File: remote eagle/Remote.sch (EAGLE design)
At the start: 13 parts, among them Y1 8MHz

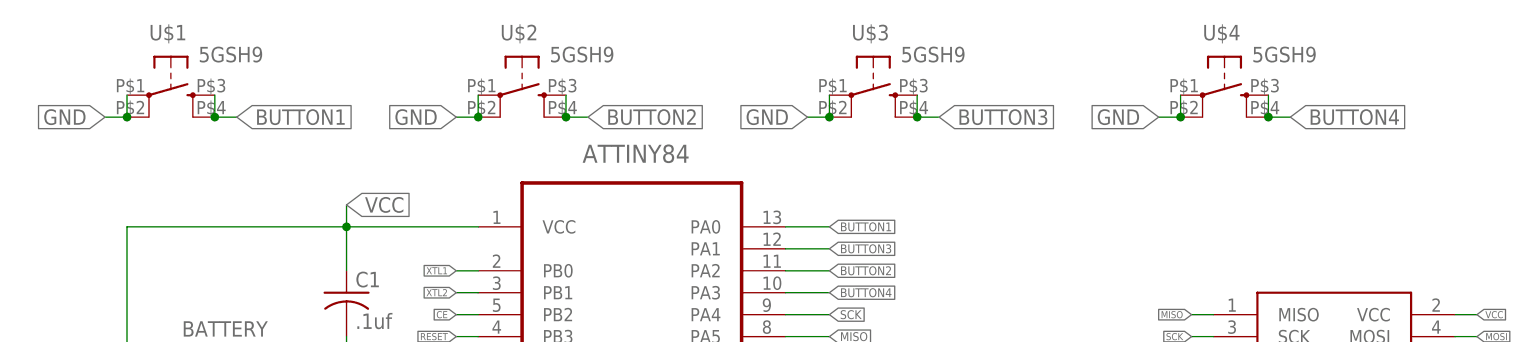
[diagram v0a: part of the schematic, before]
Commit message: Resizing board to accomodate new tactile switches. Sending to printer.
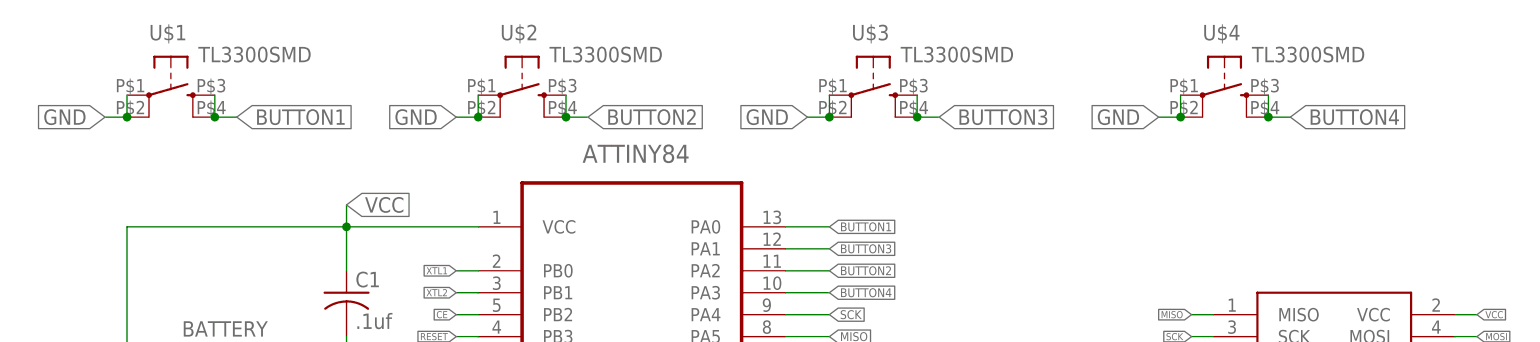
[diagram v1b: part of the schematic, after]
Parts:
- U$1, U$2, U$3, U$4: value 5GSH9 -> TL3300SMD; device remote:5GSH9 -> remote:TL3300SMD
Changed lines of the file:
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@@
 <part name="C5" library="SparkFun-Passives" deviceset="CAP" device="0805" value="15pF"/>
 <part name="C6" library="SparkFun-Passives" deviceset="CAP" device="0805" value="15pF"/>
-<part name="U$2" library="remote" deviceset="5GSH9" device=""/>
-<part name="U$3" library="remote" deviceset="5GSH9" device=""/>
-<part name="U$4" library="remote" deviceset="5GSH9" device=""/>
-<part name="U$1" library="remote" deviceset="5GSH9" device=""/>
+<part name="U$2" library="remote" deviceset="TL3300" device="SMD"/>
+<part name="U$3" library="remote" deviceset="TL3300" device="SMD"/>
+<part name="U$4" library="remote" deviceset="TL3300" device="SMD"/>
+<part name="U$1" library="remote" deviceset="TL3300" device="SMD"/>
 </parts>
 <sheets>
@@
 <instance part="C5" gate="G$1" x="17.78" y="-2.54" rot="R90"/>
 <instance part="C6" gate="G$1" x="17.78" y="-7.62" rot="R90"/>
-<instance part="U$2" gate="G$1" x="63.5" y="40.64" rot="R270"/>
-<instance part="U$3" gate="G$1" x="104.14" y="40.64" rot="R270"/>
-<instance part="U$4" gate="G$1" x="144.78" y="40.64" rot="R270"/>
-<instance part="U$1" gate="G$1" x="22.86" y="40.64" rot="R270"/>
+<instance part="U$2" gate="G$1" x="63.5" y="45.72" rot="R270"/>
+<instance part="U$3" gate="G$1" x="104.14" y="45.72" rot="R270"/>
+<instance part="U$4" gate="G$1" x="144.78" y="45.72" rot="R270"/>
+<instance part="U$1" gate="G$1" x="22.86" y="45.72" rot="R270"/>
 </instances>
 <busses>

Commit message: Rev. 5, includes new isp touch.
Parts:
- removed ISP: AVRISP-6, adafruit:AVRISP-6
- added J1: ISP Touch, remote:ISPTOUCH_HEADER
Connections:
- net GND: now also J1.6; no longer ISP.GND
- net MISO: now also J1.1; no longer ISP.MISO
- net MOSI: now also J1.4; no longer ISP.MOSI
- net RESET: now also J1.5; no longer ISP.RST
- net SCK: now also J1.3; no longer ISP.SCK
- net VCC: now also J1.2; no longer ISP.VCC
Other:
- moved on the sheet: R8
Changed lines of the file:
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@@
 <part name="ATTINY84" library="Atmel_By_element14_Batch_1" deviceset="ATTINY84-20SSU" device="" value=""/>
 <part name="C1" library="adafruit" deviceset="C-US" device="C0805" value=".1uf"/>
-<part name="ISP" library="adafruit" deviceset="AVRISP" device="-6"/>
 <part name="RADIO" library="pinhead" deviceset="PINHD-2X4" device="" value="NRF24L01"/>
 <part name="R8" library="adafruit" deviceset="R-US_" device="R0805" value="10k"/>
@@
 <part name="U$4" library="remote" deviceset="TL3300" device="SMD"/>
 <part name="U$1" library="remote" deviceset="TL3300" device="SMD"/>
+<part name="J1" library="remote" deviceset="ISPTOUCH" device="_HEADER" value="ISP Touch"/>
 </parts>
 <sheets>
@@
 <instance part="ATTINY84" gate="A" x="76.2" y="22.86"/>
 <instance part="C1" gate="G$1" x="43.18" y="20.32"/>
-<instance part="ISP" gate="G$1" x="156.21" y="15.24"/>
 <instance part="RADIO" gate="A" x="149.86" y="-5.08"/>
-<instance part="R8" gate="G$1" x="132.08" y="8.89"/>
+<instance part="R8" gate="G$1" x="127" y="15.24"/>
 <instance part="Y1" gate="G$1" x="25.4" y="-5.08" smashed="yes" rot="R90">
 <attribute name="NAME" x="26.67" y="0" size="1.778" layer="95" rot="R180"/>
@@
 <instance part="U$4" gate="G$1" x="144.78" y="45.72" rot="R270"/>
 <instance part="U$1" gate="G$1" x="22.86" y="45.72" rot="R270"/>
+<instance part="J1" gate="G$1" x="147.32" y="22.86"/>
 </instances>
 <busses>
@@
 </segment>
 <segment>
-<pinref part="ISP" gate="G$1" pin="GND"/>
-<wire x1="171.45" y1="12.7" x2="173.99" y2="12.7" width="0.1524" layer="91"/>
-<label x="173.99" y="12.7" size="0.8128" layer="95" xref="yes"/>
-</segment>
-<segment>
 <pinref part="RADIO" gate="A" pin="1"/>
 <wire x1="147.32" y1="0" x2="139.7" y2="0" width="0.1524" layer="91"/>
@@
 <pinref part="C6" gate="G$1" pin="1"/>
 </segment>
+<segment>
+<pinref part="J1" gate="G$1" pin="6"/>
+<wire x1="157.48" y1="20.32" x2="162.56" y2="20.32" width="0.1524" layer="91"/>
+<label x="162.56" y="20.32" size="1.016" layer="95" xref="yes"/>
+</segment>
 </net>
 <net name="MISO" class="0">
-<segment>
-<pinref part="ISP" gate="G$1" pin="MISO"/>
-<wire x1="143.51" y1="17.78" x2="140.97" y2="17.78" width="0.1524" layer="91"/>
-<label x="140.97" y="17.78" size="0.8128" layer="95" rot="R180" xref="yes"/>
-</segment>
 <segment>
 <pinref part="RADIO" gate="A" pin="6"/>
@@
 <label x="99.06" y="15.24" size="1.016" layer="95" xref="yes"/>
 </segment>
+<segment>
+<pinref part="J1" gate="G$1" pin="1"/>
+<wire x1="139.7" y1="25.4" x2="134.62" y2="25.4" width="0.1524" layer="91"/>
+<label x="134.62" y="25.4" size="1.016" layer="95" rot="R180" xref="yes"/>
+</segment>
 </net>
 <net name="MOSI" class="0">
-<segment>
-<pinref part="ISP" gate="G$1" pin="MOSI"/>
-<wire x1="171.45" y1="15.24" x2="173.99" y2="15.24" width="0.1524" layer="91"/>
-<label x="173.99" y="15.24" size="0.8128" layer="95" xref="yes"/>
-</segment>
 <segment>
 <pinref part="RADIO" gate="A" pin="7"/>
@@
 <label x="99.06" y="12.7" size="1.016" layer="95" xref="yes"/>
 </segment>
+<segment>
+<pinref part="J1" gate="G$1" pin="4"/>
+<wire x1="157.48" y1="22.86" x2="162.56" y2="22.86" width="0.1524" layer="91"/>
+<label x="162.56" y="22.86" size="1.016" layer="95" xref="yes"/>
+</segment>
 </net>
 <net name="SCK" class="0">
@@
 </segment>
 <segment>
-<pinref part="ISP" gate="G$1" pin="SCK"/>
-<wire x1="143.51" y1="15.24" x2="140.97" y2="15.24" width="0.1524" layer="91"/>
-<label x="140.97" y="15.24" size="0.8128" layer="95" rot="R180" xref="yes"/>
-</segment>
-<segment>
 <label x="139.7" y="-5.08" size="0.8128" layer="95" rot="R180" xref="yes"/>
 <pinref part="RADIO" gate="A" pin="5"/>
 <wire x1="139.7" y1="-5.08" x2="147.32" y2="-5.08" width="0.1524" layer="91"/>
+</segment>
+<segment>
+<pinref part="J1" gate="G$1" pin="3"/>
+<wire x1="139.7" y1="22.86" x2="134.62" y2="22.86" width="0.1524" layer="91"/>
+<label x="134.62" y="22.86" size="1.016" layer="95" rot="R180" xref="yes"/>
 </segment>
 </net>
@@
 </segment>
 <segment>
-<pinref part="ISP" gate="G$1" pin="VCC"/>
-<wire x1="171.45" y1="17.78" x2="173.99" y2="17.78" width="0.1524" layer="91"/>
-<label x="173.99" y="17.78" size="0.8128" layer="95" xref="yes"/>
-</segment>
-<segment>
 <pinref part="RADIO" gate="A" pin="2"/>
 <wire x1="154.94" y1="0" x2="162.56" y2="0" width="0.1524" layer="91"/>
@@
 </segment>
 <segment>
+<pinref part="J1" gate="G$1" pin="2"/>
+<wire x1="157.48" y1="25.4" x2="162.56" y2="25.4" width="0.1524" layer="91"/>
+<label x="162.56" y="25.4" size="1.016" layer="95" xref="yes"/>
+</segment>
+<segment>
 <pinref part="R8" gate="G$1" pin="1"/>
-<wire x1="127" y1="8.89" x2="124.46" y2="8.89" width="0.1524" layer="91"/>
-<label x="124.46" y="8.89" size="0.8128" layer="95" rot="R180" xref="yes"/>
+<wire x1="121.92" y1="15.24" x2="119.38" y2="15.24" width="0.1524" layer="91"/>
+<label x="119.38" y="15.24" size="1.016" layer="95" rot="R180" xref="yes"/>
 </segment>
 </net>
 <net name="RESET" class="0">
-<segment>
-<pinref part="ISP" gate="G$1" pin="RST"/>
-<wire x1="143.51" y1="12.7" x2="140.97" y2="12.7" width="0.1524" layer="91"/>
-<label x="140.97" y="12.7" size="0.8128" layer="95" rot="R180" xref="yes"/>
-<pinref part="R8" gate="G$1" pin="2"/>
-<wire x1="137.16" y1="8.89" x2="140.97" y2="8.89" width="0.1524" layer="91"/>
-<wire x1="140.97" y1="8.89" x2="140.97" y2="12.7" width="0.1524" layer="91"/>
-</segment>
 <segment>
 <pinref part="ATTINY84" gate="A" pin="PB3"/>
@@
 <wire x1="58.42" y1="15.24" x2="55.88" y2="15.24" width="0.1524" layer="91"/>
 </segment>
-</net>
+<segment>
+<pinref part="J1" gate="G$1" pin="5"/>
+<wire x1="139.7" y1="20.32" x2="134.62" y2="20.32" width="0.1524" layer="91"/>
+<label x="134.62" y="20.32" size="1.016" layer="95" rot="R180" xref="yes"/>
+<wire x1="134.62" y1="20.32" x2="134.62" y2="15.24" width="0.1524" layer="91"/>
+<pinref part="R8" gate="G$1" pin="2"/>
+<wire x1="134.62" y1="15.24" x2="132.08" y2="15.24" width="0.1524" layer="91"/>
+</segment>
+</net>

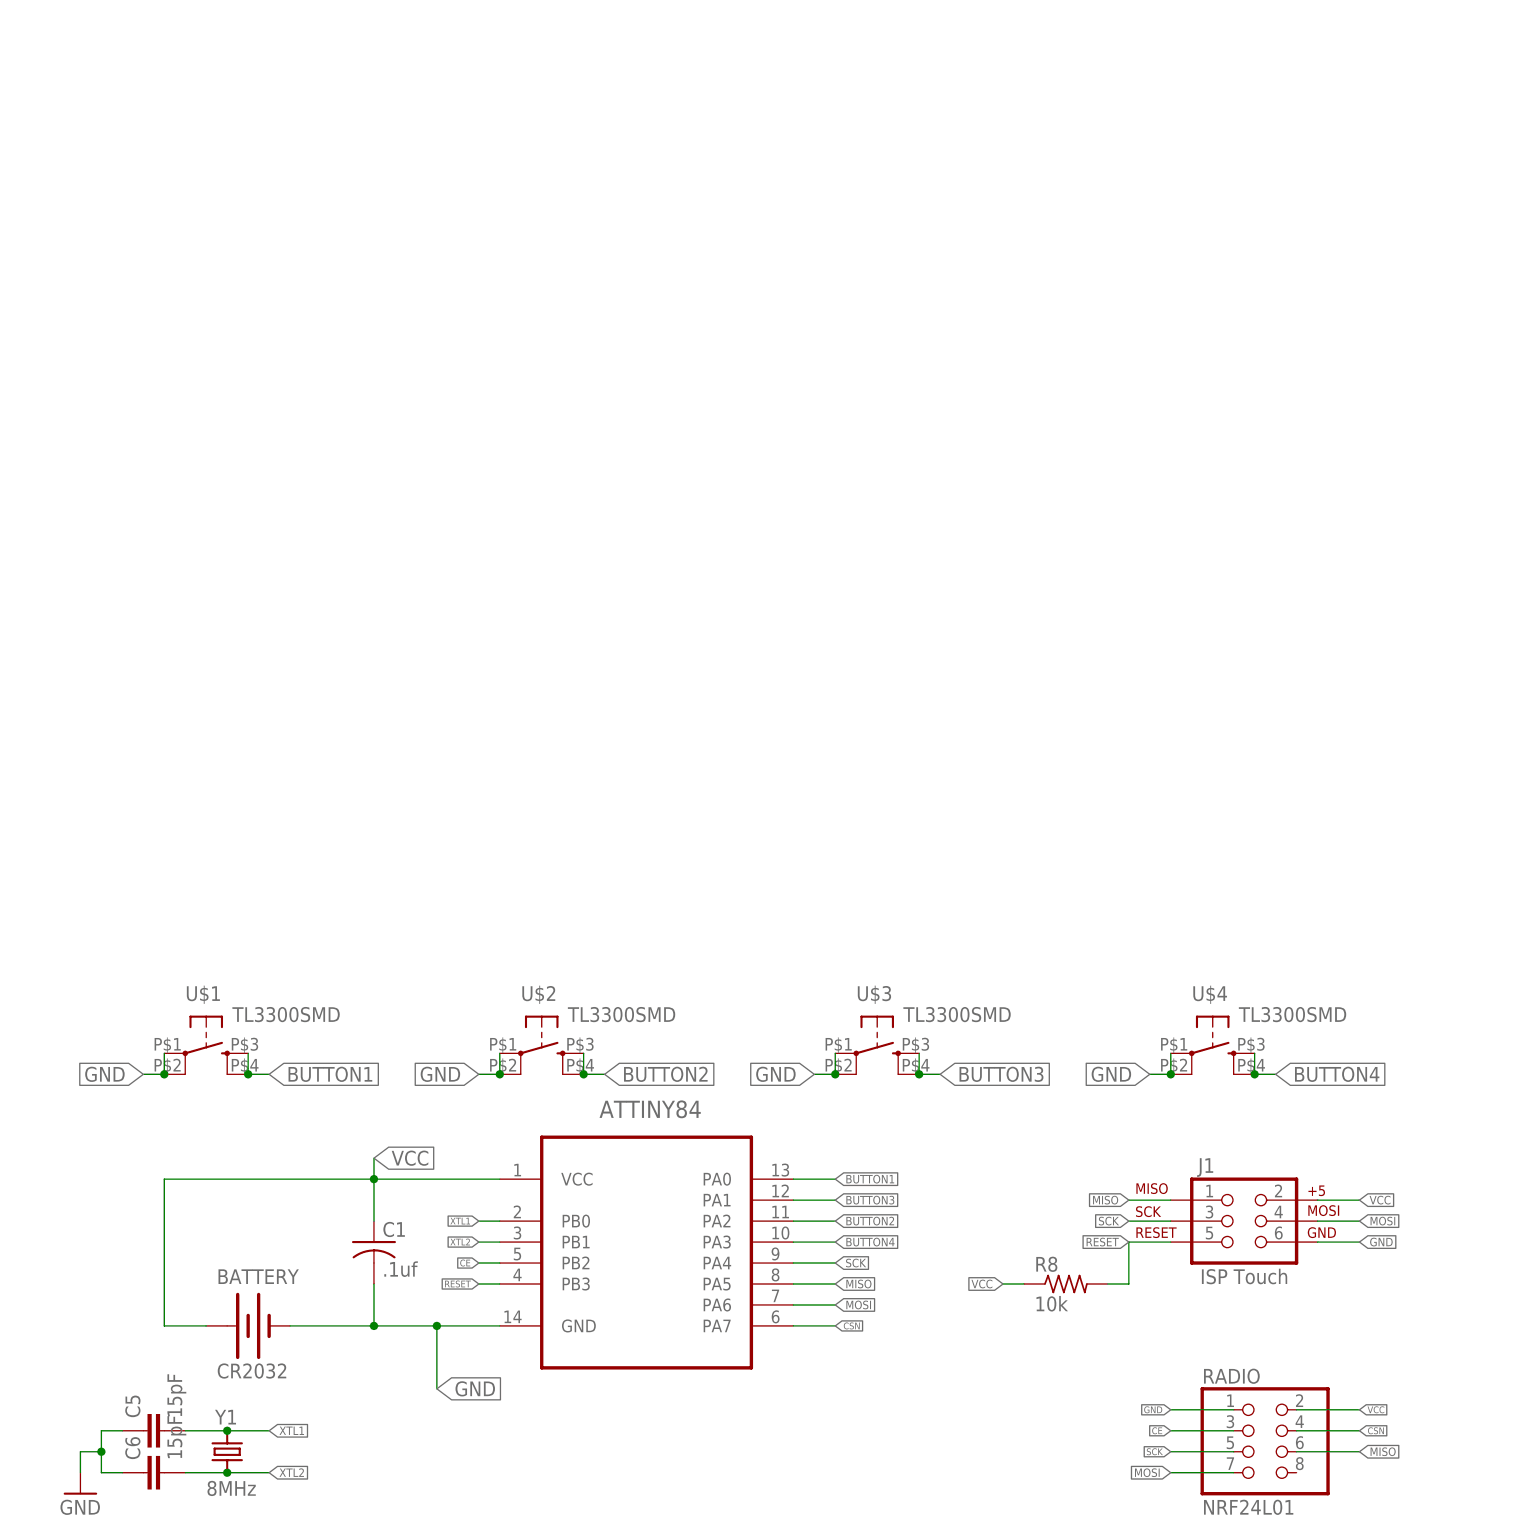
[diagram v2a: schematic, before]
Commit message: Moving from nrf24L01+ module to onboard chip. Moving both MCU and radio IC to QFN package.
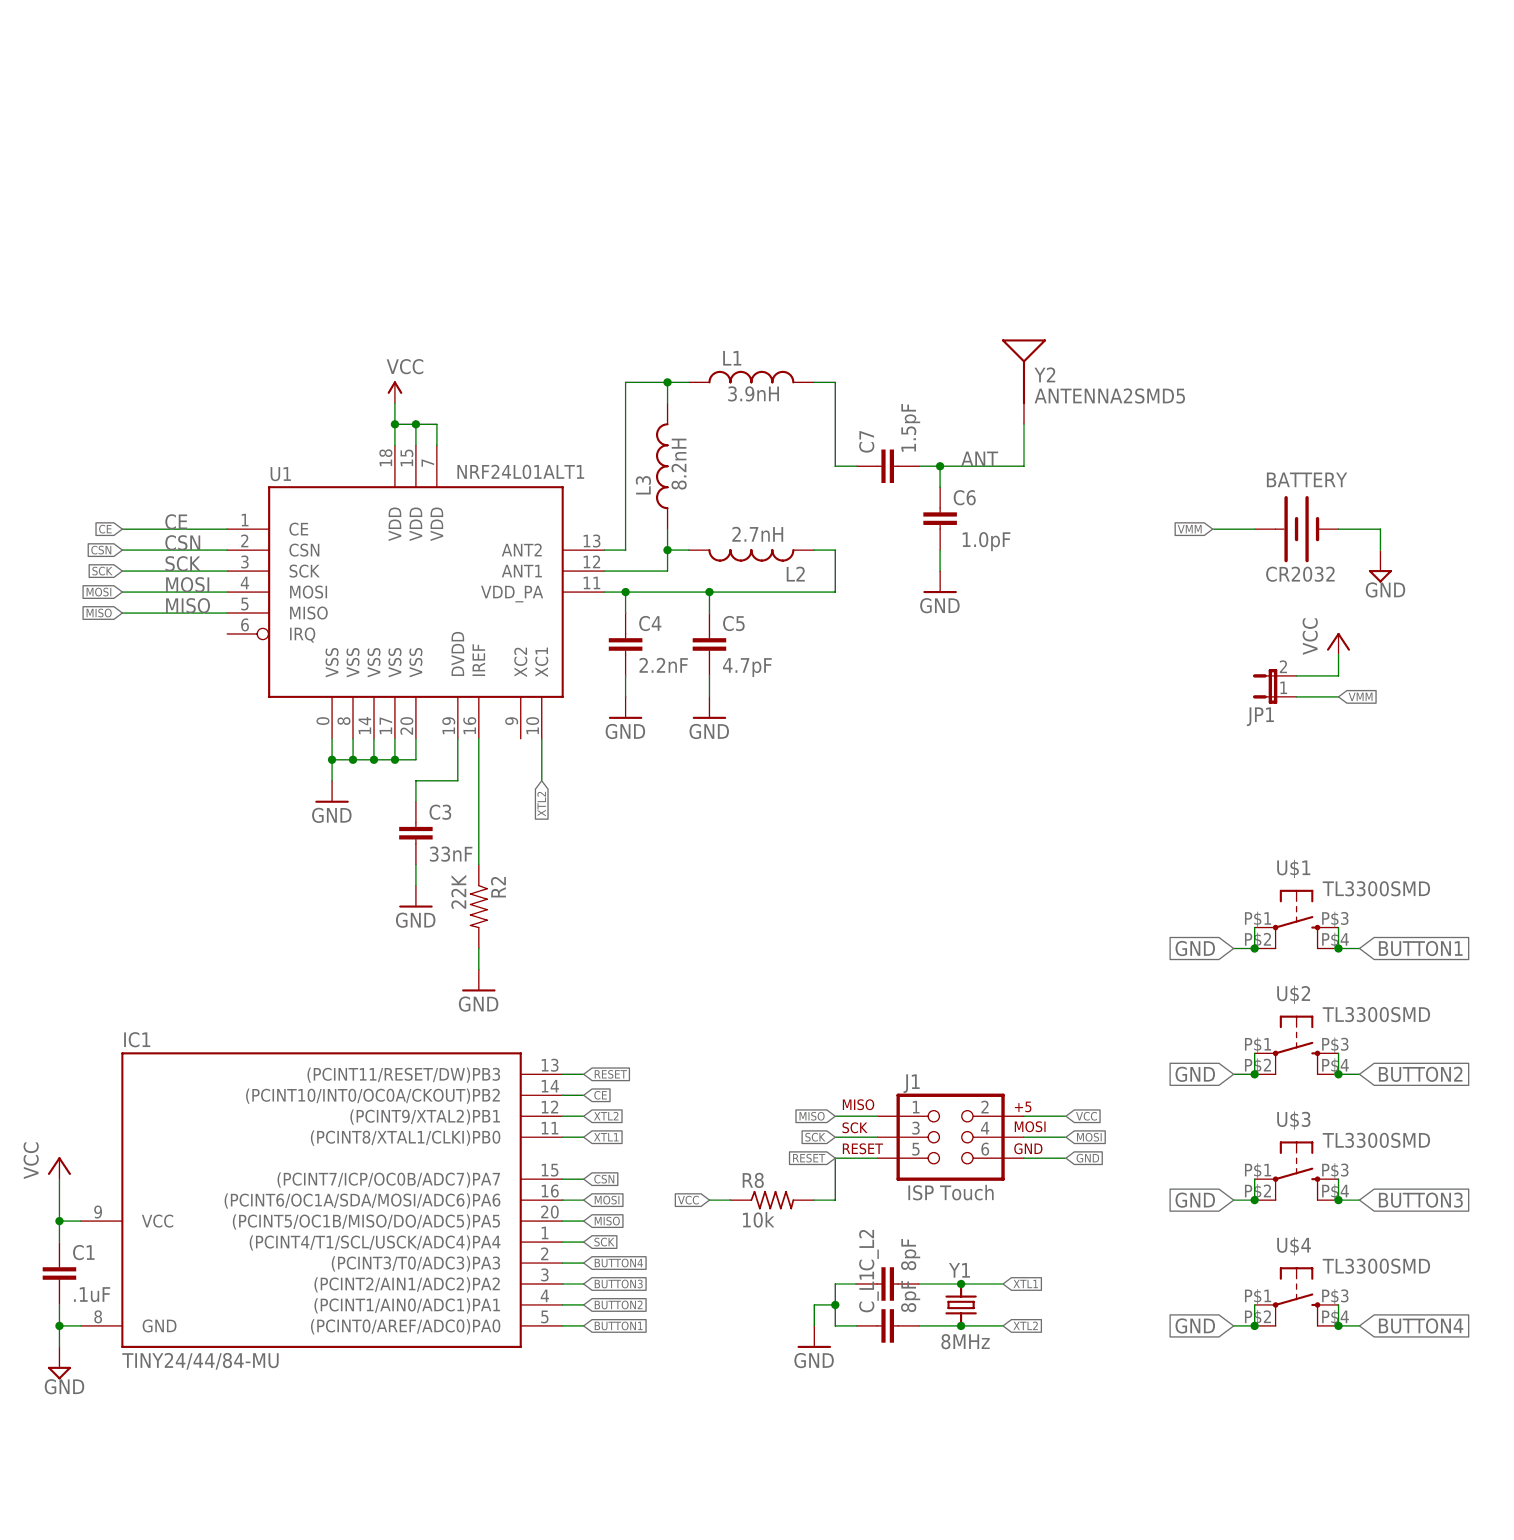
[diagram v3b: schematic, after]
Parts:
- removed ATTINY84: ATTINY84-20SSU, Atmel_By_element14_Batch_1:ATTINY84-20SSU
- removed RADIO: NRF24L01, pinhead:PINHD-2X4
- added C3: 33nF, SparkFun:CAP0402-CAP
- added C4: 2.2nF, SparkFun:CAP0402-CAP
- added C7: 1.5pF, SparkFun:CAP0402-CAP
- added C_L1, C_L2: 8pF, SparkFun-Passives:CAP0402-CAP
- added IC1: TINY24/44/84-MU, avr-7:TINY24/44/84-MU
- added JP1: (no value), SparkFun-Passives:JUMPER-2SMD-NC
- added L1: 3.9nH, SparkFun:INDUCTOR0402
- added L2: 2.7nH, SparkFun:INDUCTOR0402
- added L3: 8.2nH, SparkFun:INDUCTOR0402
- added LOGO: (no value), remote:TURNTOUCHLOGO200DPI
- added R2: 22K, SparkFun:RESISTOR0402-RES
- added U1: NRF24L01ALT1, Testing:NRF24L01ALT1
- added Y2: ANTENNA2SMD5, SparkFun:ANTENNA2SMD5
- C1: value .1uf -> .1uF; device adafruit:C-USC0805 -> SparkFun-Passives:CAP0402-CAP
- C5: value 15pF -> 4.7pF; device SparkFun-Passives:CAP0805 -> SparkFun:CAP0402-CAP
- C6: value 15pF -> 1.0pF; device SparkFun-Passives:CAP0805 -> SparkFun:CAP0402-CAP
- R8: device adafruit:R-US_R0805 -> resistor:R-US_R0402
- Y1: device remote:CRYSTAL -> remote:CRYSTAL8X4.5
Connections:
- new net ANT: C6.2, C7.2, Y2.SIGNAL
- new net N$4: R2.1, U1.IREF
- new net N$5: C3.1, U1.DVDD
- new net N$6: L1.1, L3.2, U1.ANT2
- new net N$7: C4.1, C5.1, L2.1, U1.VDD_PA
- new net N$8: L2.2, L3.1, U1.ANT1
- new net N$9: C7.1, L1.2
- new net VMM: BATTERY.+, JP1.1
- net BUTTON1: now also IC1.(PCINT0/AREF/ADC0)PA0; no longer ATTINY84.PA0
- net BUTTON2: now also IC1.(PCINT1/AIN0/ADC1)PA1; no longer ATTINY84.PA2
- net BUTTON3: now also IC1.(PCINT2/AIN1/ADC2)PA2; no longer ATTINY84.PA1
- net BUTTON4: now also IC1.(PCINT3/T0/ADC3)PA3; no longer ATTINY84.PA3
- net CE: now also IC1.(PCINT10/INT0/OC0A/CKOUT)PB2, U1.CE; no longer ATTINY84.PB2, RADIO.3
- net CSN: now also IC1.(PCINT7/ICP/OC0B/ADC7)PA7, U1.CSN; no longer ATTINY84.PA7, RADIO.4
- net GND: now also C3.2, C4.2, C5.2, C_L1.1, C_L2.1, IC1.GND, R2.2, U1.VSS@0, U1.VSS@14, U1.VSS@17, U1.VSS@20, U1.VSS@8; no longer ATTINY84.GND, C5.1, RADIO.1
- net MISO: now also IC1.(PCINT5/OC1B/MISO/DO/ADC5)PA5, U1.MISO; no longer ATTINY84.PA5, RADIO.6
- net MOSI: now also IC1.(PCINT6/OC1A/SDA/MOSI/ADC6)PA6, U1.MOSI; no longer ATTINY84.PA6, RADIO.7
- net RESET: now also IC1.(PCINT11/RESET/DW)PB3; no longer ATTINY84.PB3
- net SCK: now also IC1.(PCINT4/T1/SCL/USCK/ADC4)PA4, U1.SCK; no longer ATTINY84.PA4, RADIO.5
- net VCC: now also IC1.VCC, JP1.2, U1.VDD@15, U1.VDD@18, U1.VDD@7; no longer ATTINY84.VCC, BATTERY.+, RADIO.2
- net XTL1: now also C_L2.2, IC1.(PCINT8/XTAL1/CLKI)PB0; no longer ATTINY84.PB0, C5.2
- net XTL2: now also C_L1.2, IC1.(PCINT9/XTAL2)PB1, U1.XC1; no longer ATTINY84.PB1, C6.2
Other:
- moved on the sheet: BATTERY, C1, C5, C6, J1, R8, U$1, U$2, U$3, U$4, Y1
